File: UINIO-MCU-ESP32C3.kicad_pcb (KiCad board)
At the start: 2 copper layers, 60.1 x 20.3 mm, 45 parts, among them J1 Conn_01x15_Pin, J2 Conn_01x04_Pin, J3 Conn_01x15_Pin, SW1 复位按键, SW2 下载按键, U1 ME6211C33M5G-N, U2 W25Q128JVSSIQ, U3 ESP32-C3, U4 CH343P, Y1 40MHz

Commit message: Release UINIO-MCU-ESP32C3 version 3.6.0.
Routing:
- net GND: track 204.6 -> 204.7 mm, vias 130 -> 131

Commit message: Release UINIO-MCU-ESP32C3 version 3.6.2.
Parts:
- removed HOLE2: Hole-1mm, Uinio:Hole-1mm
- moved HOLE3 0.45 mm to (176.6, 94.2)
- moved HOLE4 0.45 mm to (176.6, 111.8)
- moved HOLE1 0.34 mm to (122.9, 95.4)
- moved HOLE5 0.25 mm to (122.9, 110.6)
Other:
- board size 60.1 x 20.3 mm -> 59.9 x 20.3 mm
- board text added: "Version 3.6.2"
- board text removed: "Version 3.6.0"

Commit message: Release UINIO-MCU-ESP32C3 version 3.6.2.
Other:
- board text added: "locked"
- board text removed: "3V3"
- board text removed: "5V"
- board text removed: "BOOT"
- board text removed: "DTR"
- board text removed: "EN"
- board text removed: "ESP32-C3"
- board text removed: "G0"
- board text removed: "G1"
- board text removed: "G10"
- board text removed: "G11"
- board text removed: "G12"
- board text removed: "G13"
- board text removed: "G18"
- board text removed: "G19"
- board text removed: "G2"
- board text removed: "G3"
- board text removed: "G4"
- board text removed: "G5"
- board text removed: "G6"
- board text removed: "G7"
- board text removed: "G8"
- board text removed: "G9"
- board text removed: "GND"
- board text removed: "RST"
- board text removed: "RTS"
- board text removed: "RXD"
- board text removed: "RXD0"
- board text removed: "SPICLK"
- board text removed: "SPICS0"
- board text removed: "SPID"
- board text removed: "SPIQ"
- board text removed: "TXD"
- board text removed: "TXD0"
- board text removed: "UINIO-MCU-ESP32C3"
- board text removed: "UinIO.com"
- board text removed: "Version 3.6.2"
- board text removed: "可选"

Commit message: Release UINIO-MCU-ESP32C3 version 3.6.2.
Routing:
- net /VDD_3.3V: track 145.0 -> 145.9 mm

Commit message: update
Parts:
- C1, U2: moved to F.Cu
- moved C1 17.0 mm to (140.0, 86.5)
- moved U2 17.0 mm to (143.7, 86.5), turned to 180 degrees
- moved USB1 9.03 mm to (116.5, 103.0)
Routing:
- net GND: track 204.6 -> 0.00 mm, vias 131 -> 0
- net /VDD_3.3V: track 145.9 -> 0.00 mm, vias 14 -> 0
- net /U0TXD: track 58.7 -> 0.00 mm, vias 2 -> 0
- net /U0RXD: track 58.5 -> 0.00 mm, vias 5 -> 0
- net /VDD_5V: track 50.0 -> 0.00 mm, vias 2 -> 0
- net /GPIO9/BOOT: track 34.1 -> 0.00 mm, vias 2 -> 0
- net /CHIP_EN: track 31.7 -> 0.00 mm, vias 6 -> 0
- net /SPICS0: track 28.0 -> 0.00 mm
- net /RTS: track 26.2 -> 0.00 mm
- net /SPIQ: track 24.2 -> 0.00 mm
- net /VDD_SPI/GPIO11: track 22.6 -> 0.00 mm
- net /DTR: track 22.5 -> 0.00 mm, vias 2 -> 0
- net /GPIO10: track 20.5 -> 0.00 mm
- net /SPICLK: track 19.2 -> 0.00 mm
- net /SPIHD/GPIO12: track 18.4 -> 0.00 mm
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- removed copper zone on B.Cu, net GND
- removed copper zone on F.Cu, net GND
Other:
- board size 59.9 x 20.3 mm -> 70 x 20.3 mm
- board text added: "3V3"
- board text added: "5V"
- board text added: "BOOT"
- board text added: "DTR"
- board text added: "EN"
- board text added: "ESP32-C3"
- board text added: "G0"
- board text added: "G1"
- board text added: "G10"
- board text added: "G11"
- board text added: "G12"
- board text added: "G13"
- board text added: "G18"
- board text added: "G19"
- board text added: "G2"
- board text added: "G3"
- board text added: "G4"
- board text added: "G5"
- board text added: "G6"
- board text added: "G7"
- board text added: "G8"
- board text added: "G9"
- board text added: "GND"
- board text added: "RST"
- board text added: "RTS"
- board text added: "RXD"
- board text added: "RXD0"
- board text added: "SPICLK"
- board text added: "SPICS0"
- board text added: "SPID"
- board text added: "SPIQ"
- board text added: "TXD"
- board text added: "TXD0"
- board text added: "UINIO-MCU-ESP32C3"
- board text added: "UinIO.com"
- board text added: "Version 3.6.2"
- board text added: "可选"
- board text removed: "locked"

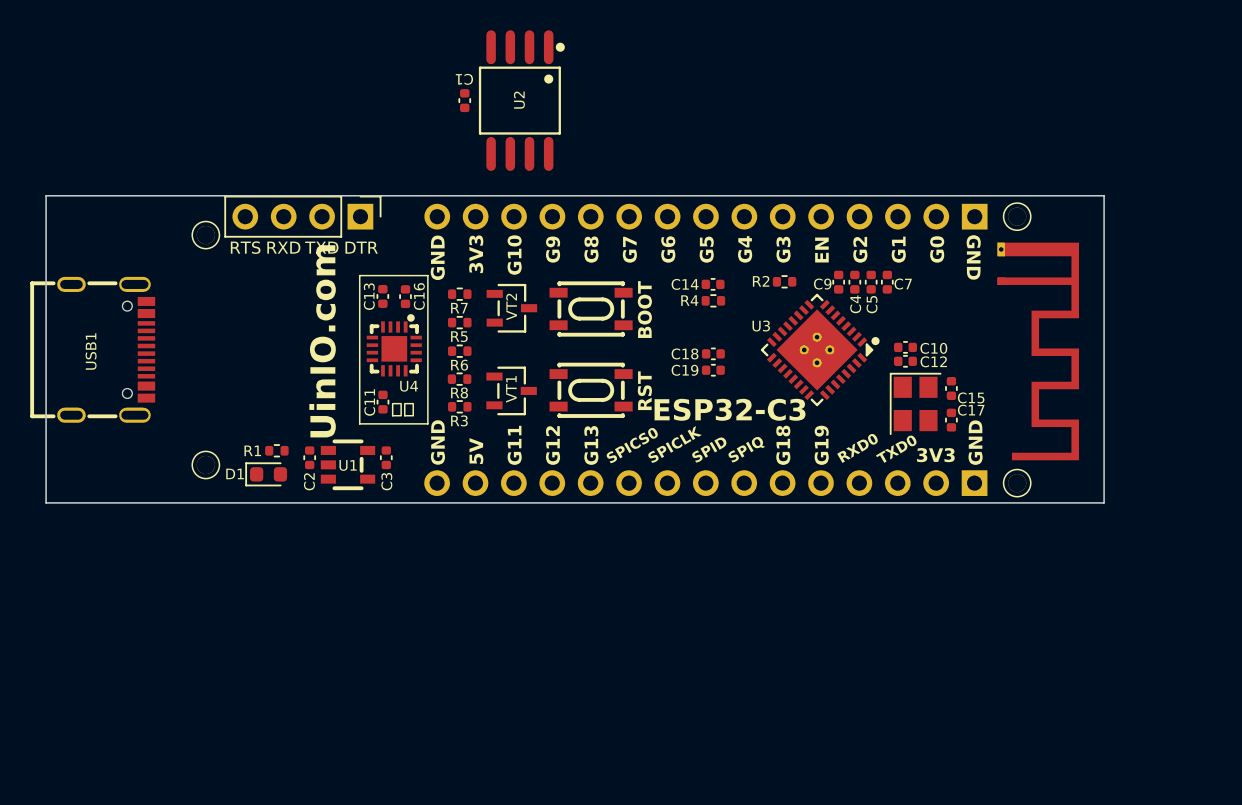
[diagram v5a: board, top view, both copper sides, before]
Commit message: Replace PCB layout.
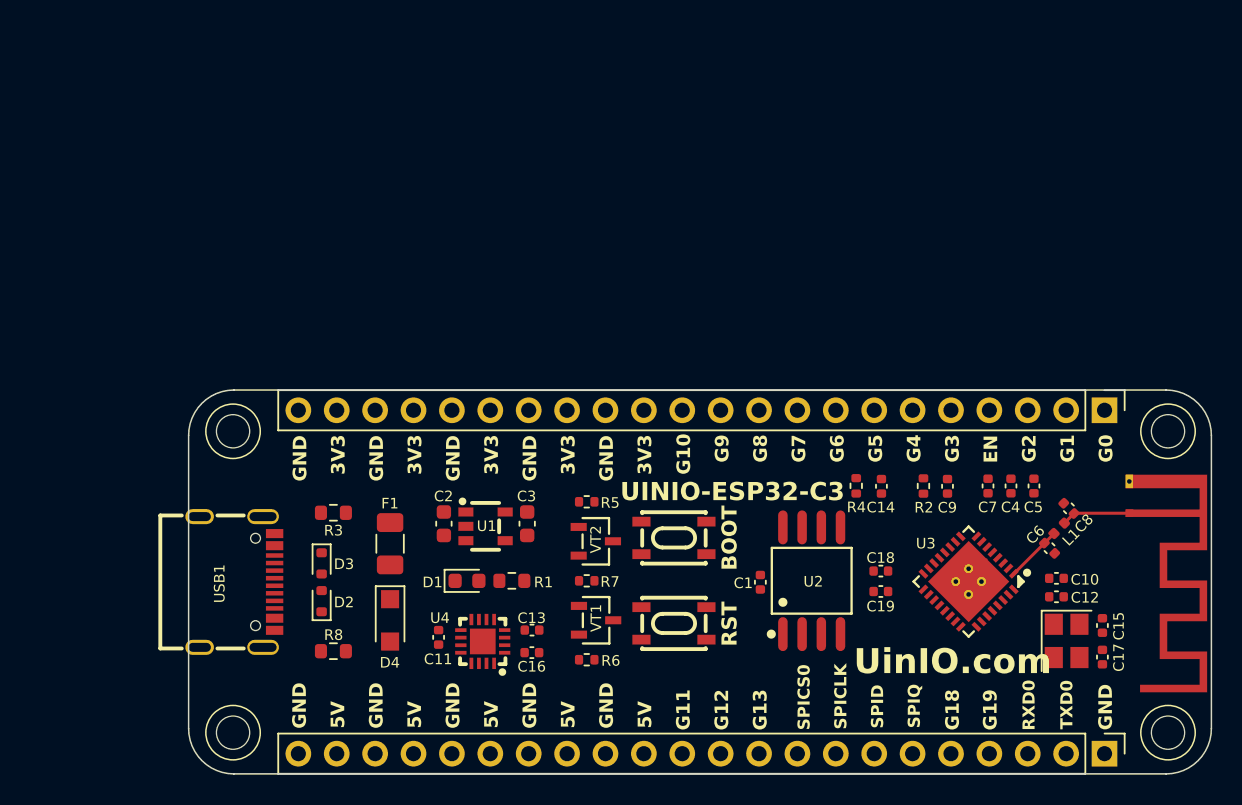
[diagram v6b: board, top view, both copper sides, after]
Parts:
- removed HOLE1, HOLE3, HOLE4, HOLE5: Hole-1mm, Uinio:Hole-1mm
- removed J3: Conn_01x15_Pin, Connector_PinHeader_2.54mm:PinHeader_1x15_P2.54mm_Vertical
- added C6: NC, Capacitor_SMD:C_0402_1005Metric, F.Cu at (178.7, 116.1)
- added C8: NC, Capacitor_SMD:C_0402_1005Metric, F.Cu at (180.0, 113.5)
- added D2: LESD5D5.0CT1G, Diode_SMD:D_SOD-523, F.Cu at (130.5, 119.6)
- added D3: LESD5D5.0CT1G, Diode_SMD:D_SOD-523, F.Cu at (130.5, 117.1)
- added D4: 1N4007, Diode_SMD:Nexperia_CFP3_SOD-123W, F.Cu at (135.1, 120.9)
- added F1: 60V 2A, Fuse:Fuse_1206_3216Metric, F.Cu at (135.1, 115.8)
- added HOLE**: Hole-2mm, Uinio:Hole-2mm, F.Cu at (186.5, 108.4)
- added HOLE**: Hole-2mm, Uinio:Hole-2mm, F.Cu at (124.7, 128.3)
- added HOLE**: Hole-2mm, Uinio:Hole-2mm, F.Cu at (186.5, 128.3)
- added HOLE**: Hole-2mm, Uinio:Hole-2mm, F.Cu at (124.7, 108.4)
- added L1: L, Inductor_SMD:L_0402_1005Metric, F.Cu at (179.3, 114.8)
- C2, C3: footprint Capacitor_SMD:C_0402_1005Metric -> Capacitor_SMD:C_0603_1608Metric
- J1: value Conn_01x15_Pin -> Conn_01x22_Pin; footprint Connector_PinHeader_2.54mm:PinHeader_1x15_P2.54mm_Vertical -> Connector_PinHeader_2.54mm:PinHeader_1x22_P2.54mm_Vertical; moved to F.Cu
- J2: value Conn_01x04_Pin -> Conn_01x22_Pin; footprint Connector_PinHeader_2.54mm:PinHeader_1x04_P2.54mm_Vertical -> Connector_PinHeader_2.54mm:PinHeader_1x22_P2.54mm_Vertical
- R1, R3, R8: footprint Resistor_SMD:R_0402_1005Metric -> Resistor_SMD:R_0603_1608Metric
- moved J2 60.7 mm to (182.3, 129.7)
- moved C1 37.4 mm to (159.6, 118.3)
- moved U2 37.2 mm to (163.0, 118.2), turned to 0 degrees
- moved C16 25.0 mm to (144.4, 123.0), turned to 0 degrees
- moved C13 24.2 mm to (144.4, 121.5), turned to 180 degrees
- moved R6 22.1 mm to (148.1, 123.5)
- moved R7 20.7 mm to (148.1, 118.3)
- moved U4 20.2 mm to (141.2, 122.3), turned to 90 degrees
- moved R8 19.8 mm to (131.3, 122.9)
- moved C15 18.6 mm to (182.2, 121.2)
- moved C17 18.6 mm to (182.2, 123.3)
- moved Y1 18.6 mm to (179.8, 122.2)
- moved C12 18.5 mm to (179.2, 119.3)
- moved C19 18.4 mm to (167.5, 119.0)
- moved U3 18.3 mm to (173.3, 118.3)
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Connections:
- J1 pad 1: GND -> /GPIO0
- J1 pad 10: /GPIO7 -> /GPIO8
- J1 pad 11: /GPIO8 -> /GPIO9/BOOT
- J1 pad 12: /GPIO9/BOOT -> /GPIO10
- J1 pad 13: /GPIO10 -> /VDD_3.3V
- J1 pad 14: /VDD_3.3V -> GND
- J1 pad 15: GND -> /VDD_3.3V
- J1 pad 2: /GPIO0 -> /GPIO1
- J1 pad 3: /GPIO1 -> /GPIO2
- J1 pad 4: /GPIO2 -> /CHIP_EN
- J1 pad 5: /CHIP_EN -> /GPIO3
- J1 pad 6: /GPIO3 -> /GPIO4
- J1 pad 7: /GPIO4 -> /GPIO5
- J1 pad 8: /GPIO5 -> /GPIO6
- J1 pad 9: /GPIO6 -> /GPIO7
- J2 pad 1: /DTR -> GND
- J2 pad 4: /RTS -> /GPIO19/USB_D+
- U3 pad 1: Net-(AE1-FEED) -> Net-(U3-LNA_IN)
- USB1 pad A4B9: /VDD_5V -> Net-(F1-Pad2)
- USB1 pad B4A9: /VDD_5V -> Net-(F1-Pad2)
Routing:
- net Net-(AE1-FEED): track 0.00 -> 4.54 mm
- net Net-(U3-LNA_IN): track 0.00 -> 3.81 mm
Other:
- board size 70 x 20.3 mm -> 67.7 x 25.4 mm
- board text added: "UINIO-ESP32-C3"
- board text removed: "DTR"
- board text removed: "ESP32-C3"
- board text removed: "RTS"
- board text removed: "RXD"
- board text removed: "TXD"
- board text removed: "可选"

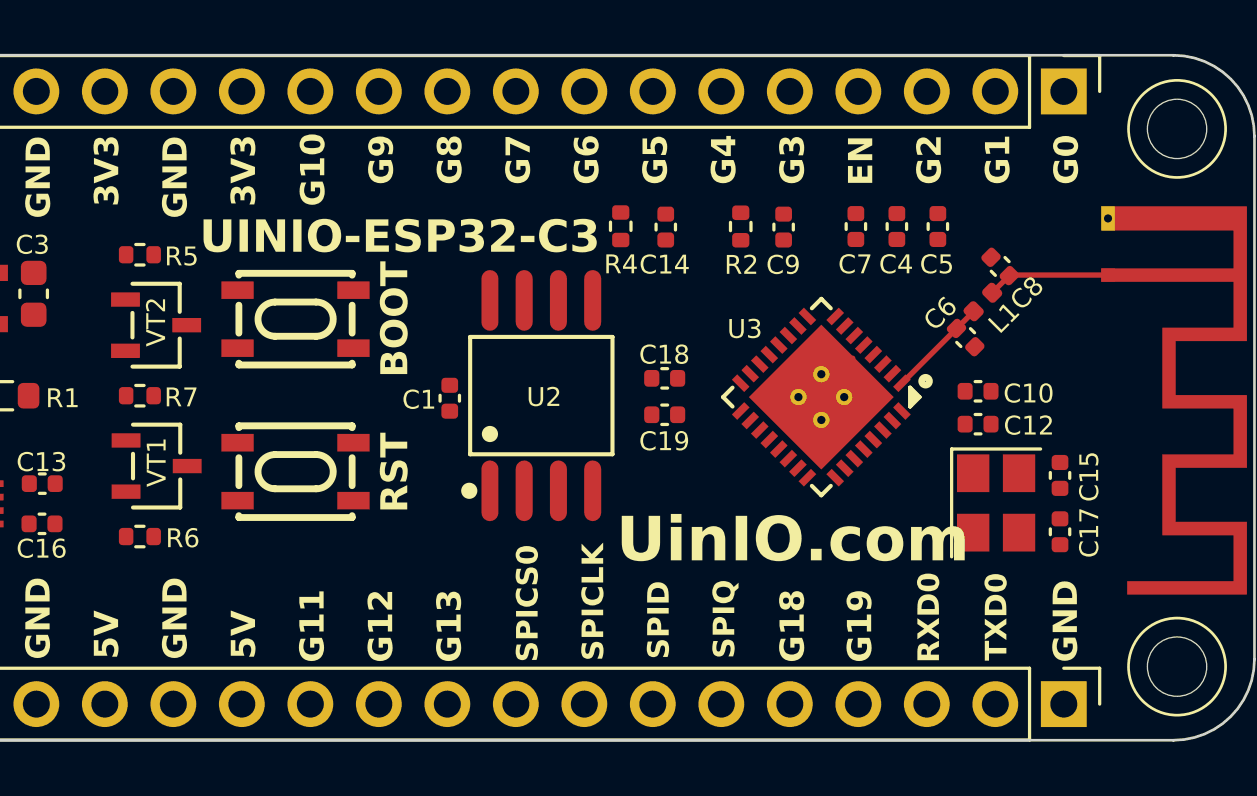
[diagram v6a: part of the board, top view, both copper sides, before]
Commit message: Replace PCB layout.
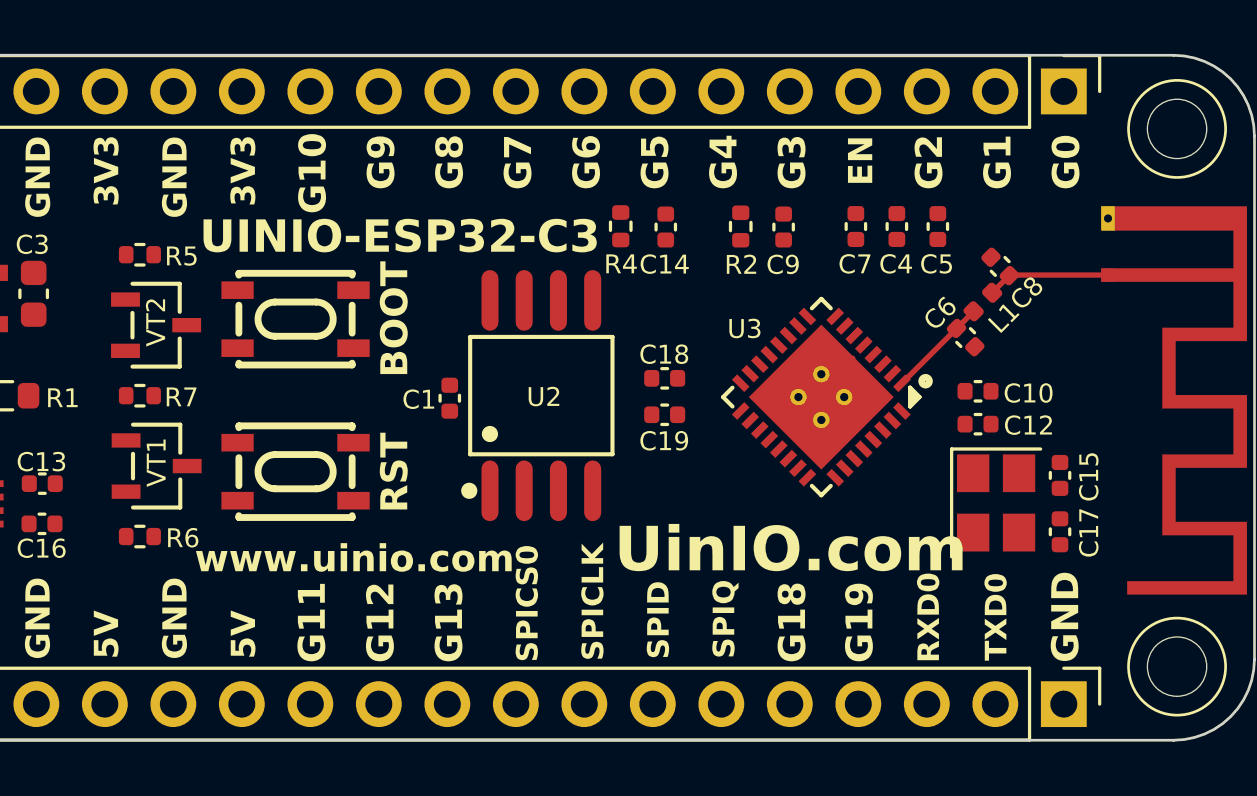
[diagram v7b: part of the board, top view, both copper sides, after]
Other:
- board text added: "www.uinio.com"
